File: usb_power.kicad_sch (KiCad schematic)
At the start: 37 parts, among them J1 USB_C_Receptacle_USB2.0_14P, Q1 IRLML6402, SW25 SW_Push_DPDT, U12 CH340N, U13 TP4056-42-ESOP8, U14 SX1308, U15 LM393

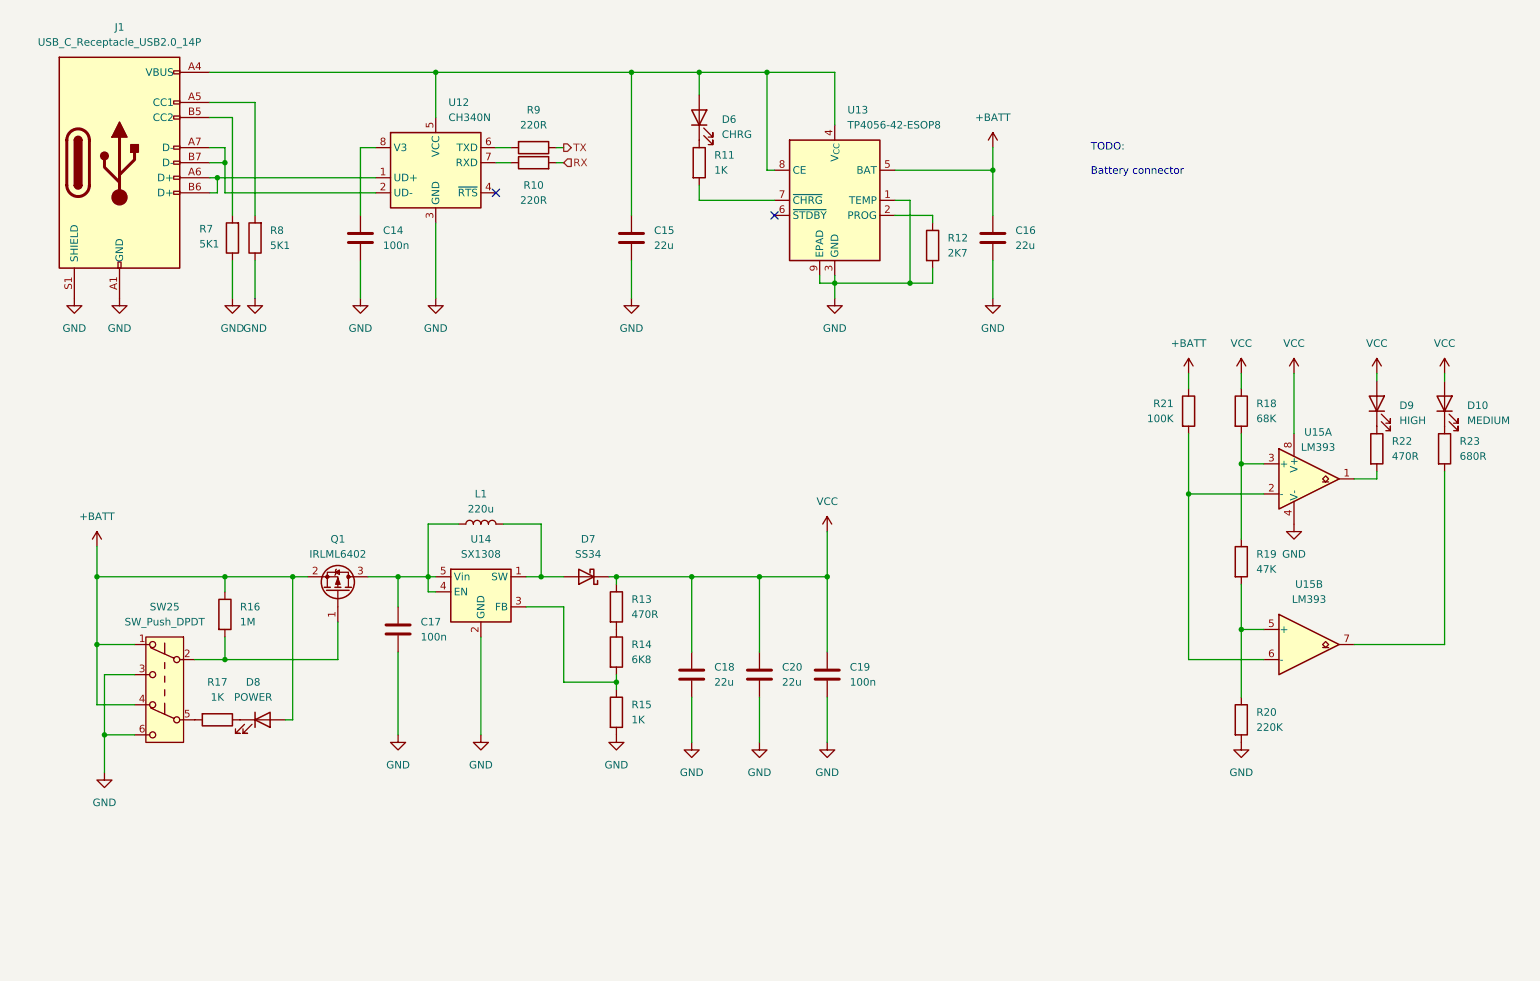
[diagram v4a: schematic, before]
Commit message: HW: Add display, start PCB placement
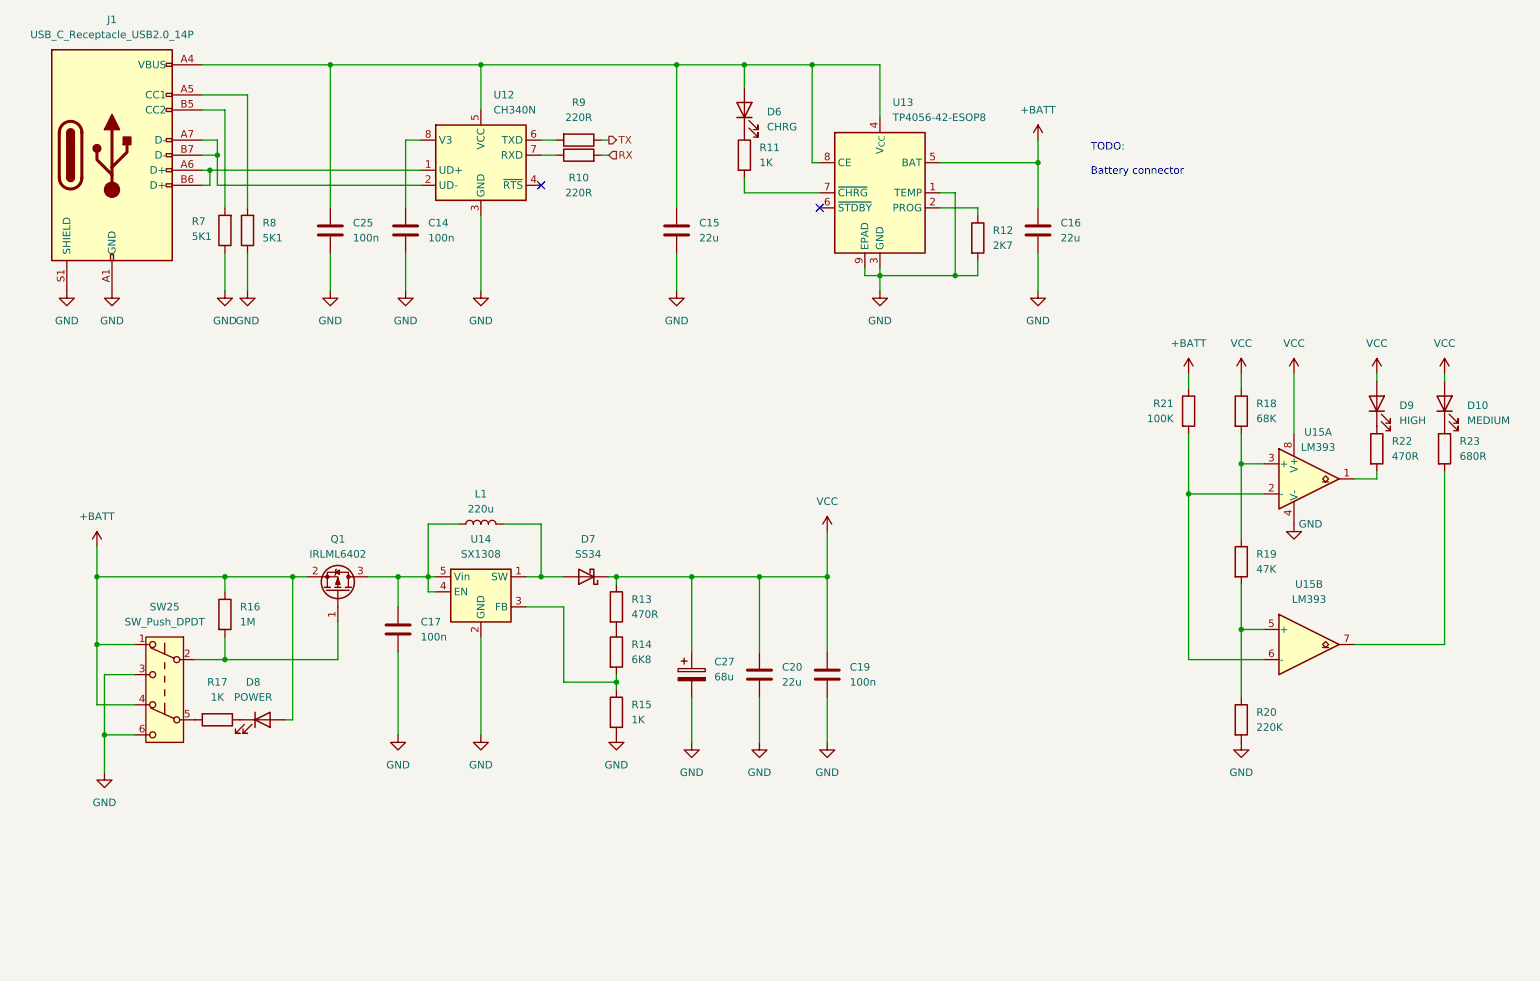
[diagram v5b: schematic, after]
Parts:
- removed C18: 22u, Capacitor_SMD:C_0805_2012Metric, symbol Device:C
- added C25: 100n, Capacitor_SMD:C_0805_2012Metric, symbol Device:C
- added C27: 68u, Capacitor_Tantalum_SMD:CP_EIA-7343-15_Kemet-W, symbol Device:C_Polarized
- J1: footprint (none) -> Connector_USB:USB_C_Receptacle_G-Switch_GT-USB-7010ASV
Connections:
- net GND: now also C25.2, C27.2
- net VCC: now also C27.1
- net at C15.1, D6.2 (A), J1.A4 (VBUS)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: now also C25.1
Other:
- moved on the sheet: C14, C15, C16, D6, J1, R10, R11, R12, R7, R8, R9, U12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

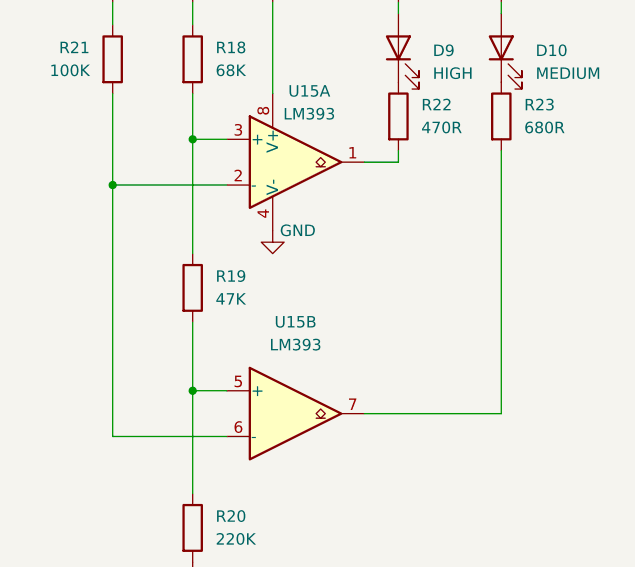
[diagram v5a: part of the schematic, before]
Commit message: HW: Add rst button, sync pins
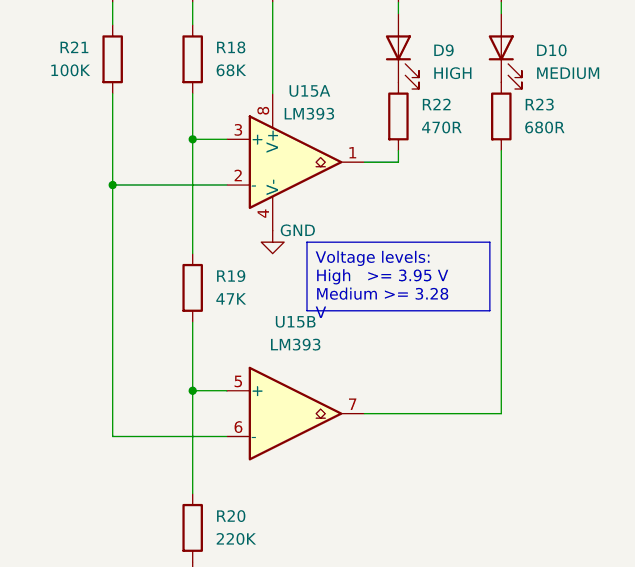
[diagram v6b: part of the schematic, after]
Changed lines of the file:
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@@
+		)
+	)
+	(text_box "Voltage levels:\nHigh   >= 3.95 V\nMedium >= 3.28 V"
+		(exclude_from_sim no)
+		(at 241.3 110.49 0)
+		(size 20.32 7.62)
+		(margins 0.9525 0.9525 0.9525 0.9525)
+		(stroke
+			(width 0)
+			(type solid)
+		)
+		(fill
+			(type none)
+		)
+		(effects
+			(font
+				(face "DM Mono")
+				(size 1.27 1.27)
+			)
+			(justify left top)
 		)
 	)

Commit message: HW: PIO done
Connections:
- net VBUS: now reaches C15.1, C25.1, D6.2 (A), J1.A4 (VBUS), J1.A9 (VBUS), J1.B4 (VBUS), J1.B9 (VBUS), U12.5 (VCC), U13.4 (V_{CC}), U13.8 (CE)
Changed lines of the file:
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@@
 	(title_block
 		(title "USB and power management")
-		(date "2025-10-14")
+		(date "2025-10-16")
 		(rev "A")
 		(company "A.K.")
@@
 	)
 	(junction
+		(at 167.64 31.75)
+		(diameter 0)
+		(color 0 0 0 0)
+	)
+	(junction
 		(at 135.89 118.11)
 		(diameter 0)
@@
 		(pts
 			(xy 156.21 31.75) (xy 167.64 31.75)
+		)
+		(stroke
+			(width 0)
+			(type default)
+		)
+	)
+	(wire
+		(pts
+			(xy 167.64 29.21) (xy 167.64 31.75)
 		)
 		(stroke
@@
 					(unit 1)
 				)
+			)
+		)
+	)
+	(symbol
+		(lib_id "power:VBUS")
+		(at 167.64 29.21 0)
+		(unit 1)
+		(exclude_from_sim no)
+		(in_bom yes)
+		(on_board yes)
+		(dnp no)
+		(fields_autoplaced yes)
+		(property "Reference" "#PWR0127"
+			(at 167.64 33.02 0)
+			(effects
+				(font
+					(size 1.27 1.27)
+				)
+				(hide yes)
+			)
+		)
+		(property "Value" "VBUS"
+			(at 167.64 24.13 0)
+			(effects
+				(font
+					(size 1.27 1.27)
+				)
+			)
+		)
+		(property "Footprint" ""
+			(at 167.64 29.21 0)
+			(effects
+				(font
+					(size 1.27 1.27)
+				)
+				(hide yes)
+			)
+		)
+		(property "Datasheet" ""
+			(at 167.64 29.21 0)
+			(effects
+				(font
+					(size 1.27 1.27)
+				)
+				(hide yes)
+			)
+		)
+		(property "Description" "Power symbol creates a global label with name \"VBUS\""
+			(at 167.64 29.21 0)
+			(effects
+				(font
+					(size 1.27 1.27)
+				)
+				(hide yes)
+			)
+		)
+		(pin "1"
+		)
+		(instances
+			(project ""
+				(path "/328c075d-c706-4d2d-bd37-a88a0c604482/c1e7a431-6e5f-4fa2-b435-dab397db0168"
+					(reference "#PWR0127")
+					(unit 1)
+				)

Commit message: HW: Start final placement
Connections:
- net +BATT: no longer D8.2 (A)
- net GND: now also R17.2
- net VCC: now also D8.2 (A)
- net at SW25.5 (B): now also Q1.1 (G), R16.2, SW25.2 (B); no longer R17.2
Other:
- moved on the sheet: D10, D8, D9, R17, R18, R19, R20, R21, R22, R23, U15A, U15B
